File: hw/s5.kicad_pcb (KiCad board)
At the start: 4 copper layers, 130 x 80 mm, 218 parts, among them J1 Conn_01x03, J12 USB_C_Receptacle, J2 LPJG0926HENL, J3 LPJG0926HENL, J4 LPJG0926HENL, J5 LPJG0926HENL, J6 LPJG0926HENL, J7 Conn_01x03, J8 microSD, Q1 NMOS, Q2 NMOS, Q3 NMOS, Q4 NMOS, Q5 NMOS, SW2 SW_Push, U1 KSZ9477S, U10 TPS3823, U11 TLV62569, U12 AP2112K-1.8, U13 TPS23861, U14 LM5122, U2 AMS1117-3.3, U3 AP2112K-2.5, U4 AP2112K-1.2, U6 TPS54560, U7 T113-S3, U8 W25N02JWZEIF, U9 TPS23861, Y1 25MHz, Y2 24MHz, Y3 32.768kHz

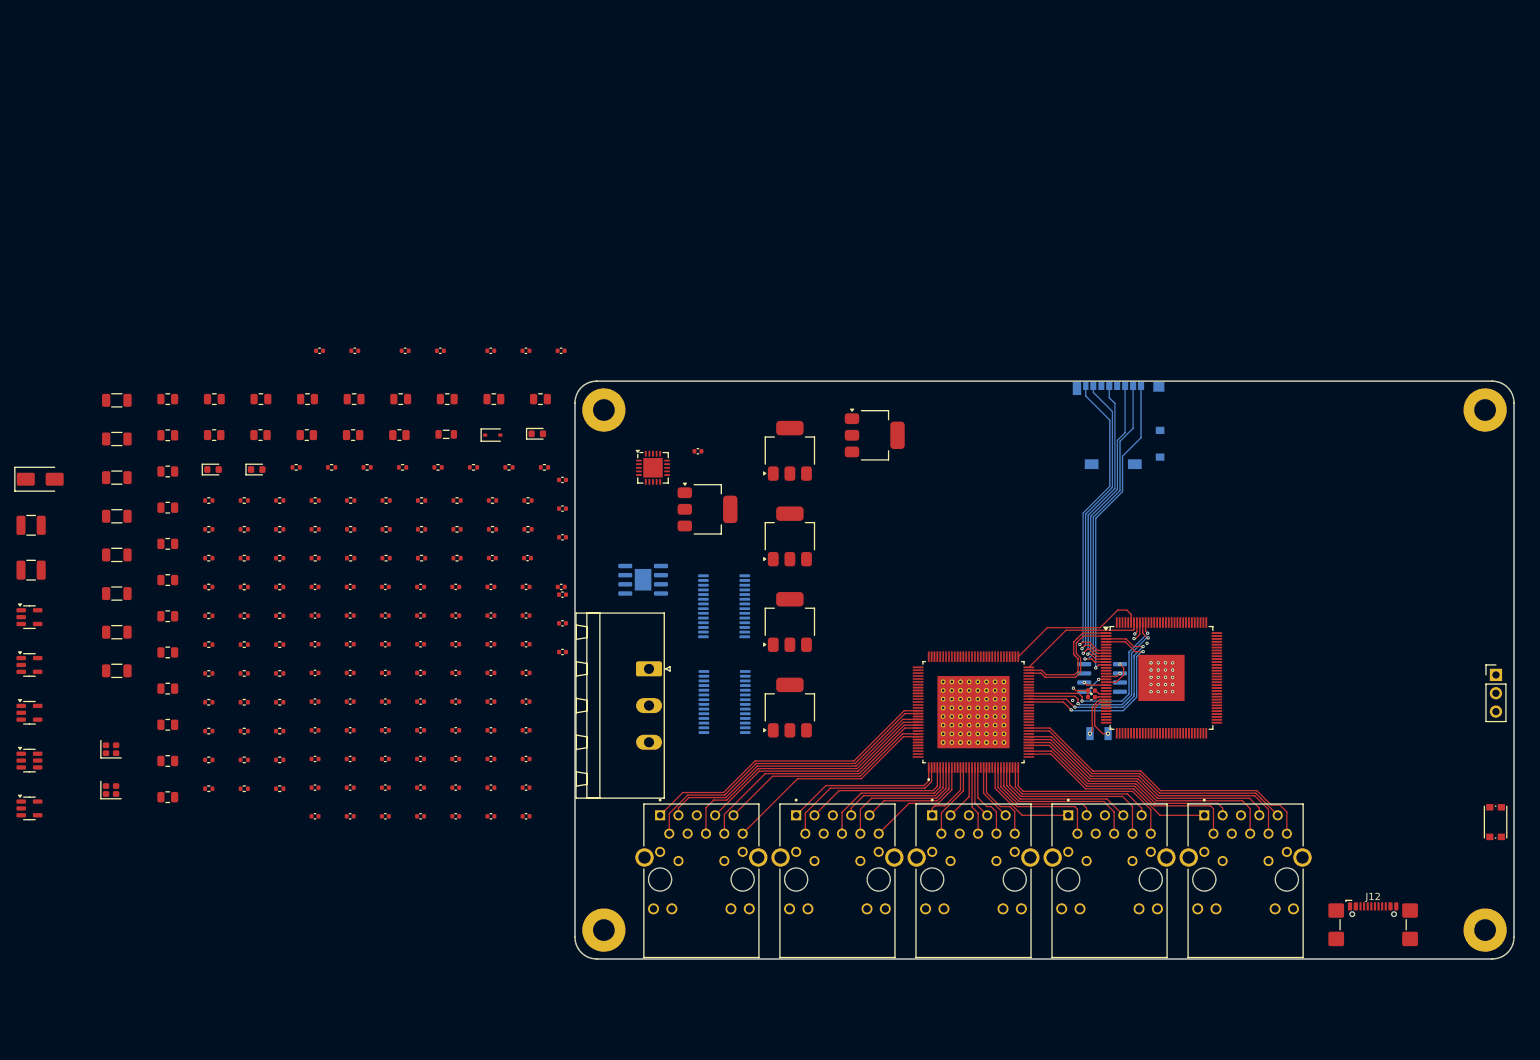
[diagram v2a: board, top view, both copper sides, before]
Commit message: hw: normalize vendor 3D models, self-contained vendor-3d/, KiCad 10 migration
- All connector/chip STEP models rotated upright and origin-corrected
- Custom models moved to vendor-3d/ with ${KIPRJMOD} paths (portable)
- Board opened/saved in KiCad 10; pre-10 backup kept as s5.kicad_pcb.bak-pre-k10
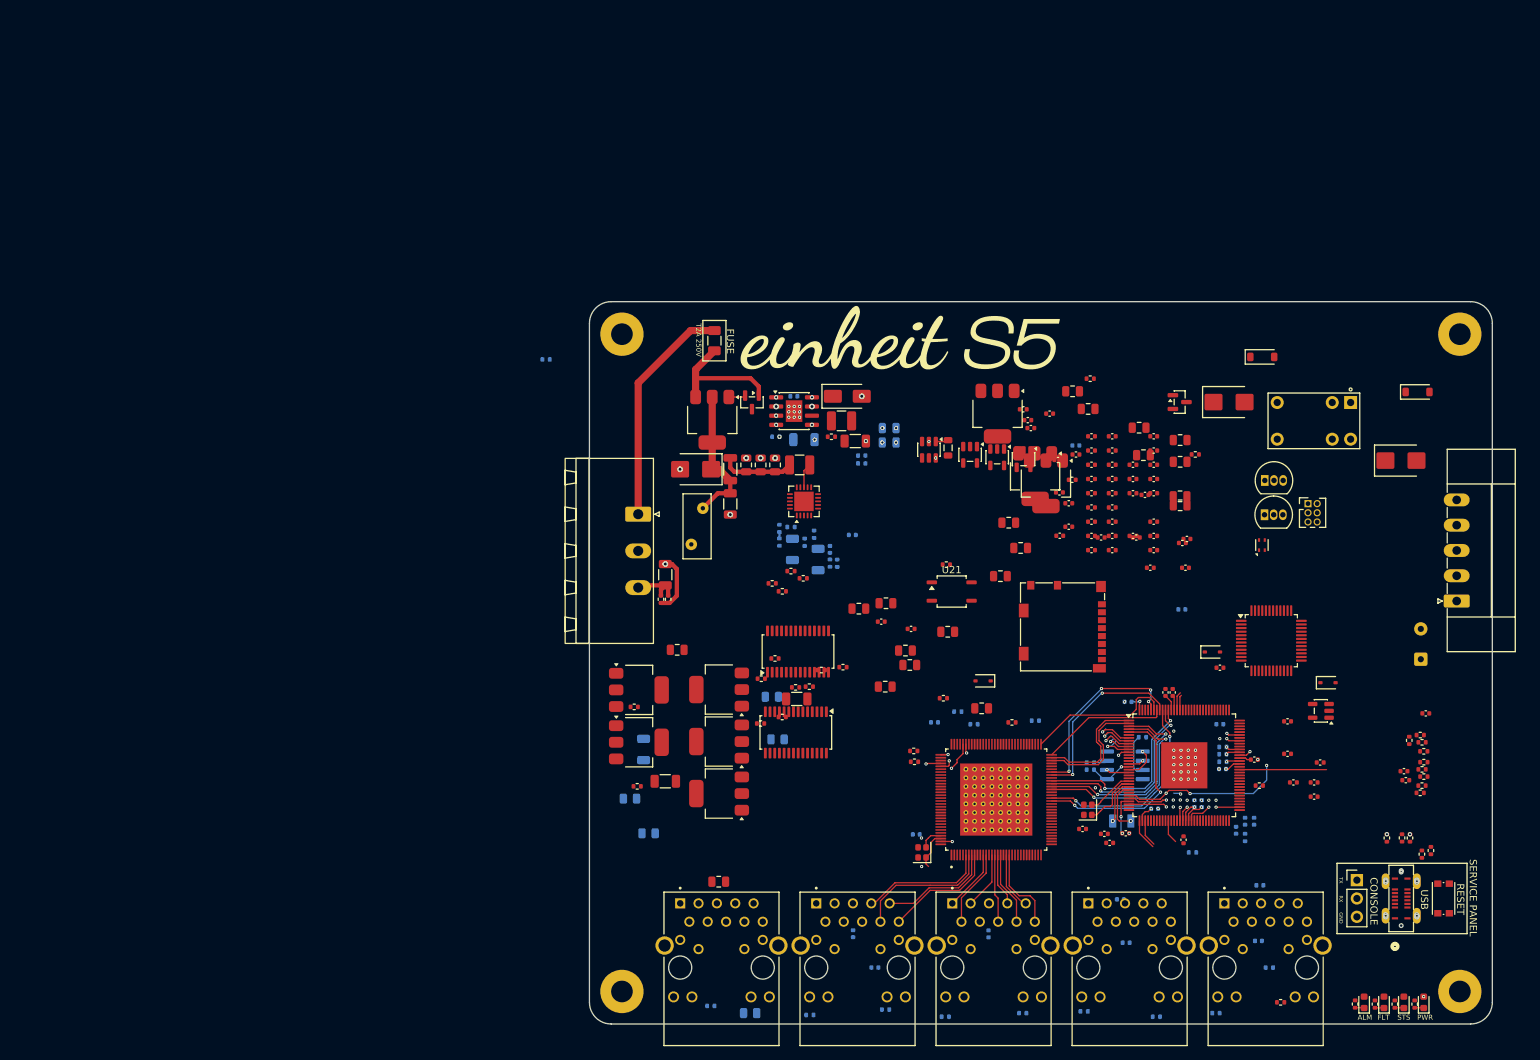
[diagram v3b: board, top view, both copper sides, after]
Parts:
- removed REF** (x4): MountingHole_3mm_Pad, MountingHole:MountingHole_3mm_Pad
- added C111: 100nF, Capacitor_SMD:C_0402_1005Metric, F.Cu at (160.8, 86.4)
- added C112: 100nF, Capacitor_SMD:C_0402_1005Metric, F.Cu at (167.6, 87.4)
- added C113: 10uF, Capacitor_SMD:C_0805_2012Metric, F.Cu at (167.3, 76.2)
- added C114: 100nF, Capacitor_SMD:C_0402_1005Metric, F.Cu at (163.6, 72.6)
- added C115: 10uF, Capacitor_SMD:C_0805_2012Metric, F.Cu at (152.4, 66.4)
- added C116: 100nF, Capacitor_SMD:C_0402_1005Metric, F.Cu at (163.6, 74.6)
- added C117: 100nF, Capacitor_SMD:C_0402_1005Metric, F.Cu at (163.6, 76.6)
- added C118: 100nF, Capacitor_SMD:C_0402_1005Metric, F.Cu at (163.6, 78.5)
- added C119: 100nF, Capacitor_SMD:C_0402_1005Metric, F.Cu at (163.6, 80.5)
- added C120: 4.7uF, Capacitor_SMD:C_0805_2012Metric, F.Cu at (167.3, 82.2)
- added C121: 100nF, Capacitor_SMD:C_0402_1005Metric, F.Cu at (198.5, 120.2)
- added C122: 100nF, Capacitor_SMD:C_0402_1005Metric, F.Cu at (163.6, 84.5)
- added C123: 100nF, Capacitor_SMD:C_0402_1005Metric, F.Cu at (163.6, 86.4)
- added C124: 100nF, Capacitor_SMD:C_0402_1005Metric, F.Cu at (163.6, 88.4)
- added C125: 4.7nF, Capacitor_SMD:C_1206_3216Metric, F.Cu at (96.0, 91.8)
- added D50: SMBJ30A, Diode_SMD:D_SMB, F.Cu at (100.2, 77.2)
- added D51: BZX84C12, Package_TO_SOT_SMD:SOT-23, F.Cu at (108.0, 67.9)
- added D52: BAT54, Diode_SMD:D_SOD-323, F.Cu at (171.8, 102.5)
- added D53: BAT54, Diode_SMD:D_SOD-323, F.Cu at (187.8, 106.8)
- added D54: 1N4148W, Diode_SMD:D_SOD-123, F.Cu at (200.2, 66.5)
- added D55: SMBJ33CA, Diode_SMD:D_SMB, F.Cu at (174.1, 67.9)
- added D56: 1N4148W, Diode_SMD:D_SOD-123, F.Cu at (178.7, 61.6)
- added D57: SMBJ33CA, Diode_SMD:D_SMB, F.Cu at (197.8, 76.0)
- added D6: LED, LED_SMD:LED_0603_1608Metric, F.Cu at (192.8, 151.0)
- added F1: Fuse_2A_TL, Fuse:Fuse_1206_3216Metric, F.Cu at (102.8, 59.4)
- added FB1: BLM31PG601SN1, Inductor_SMD:L_1206_3216Metric, F.Cu at (105.0, 77.2)
- added J10: SWD_2x3, Connector_PinHeader_1.27mm:PinHeader_2x03_P1.27mm_Vertical, F.Cu at (185.0, 82.0)
- added J11: MC1,5/5-GF-3,5_1843826, Connector_Phoenix_MC:PhoenixContact_MC_1,5_5-GF-3.5_1x05_P3.50mm_Horizontal_ThreadedFlange, F.Cu at (205.6, 95.4)
- added K1: HFD23-024-1ZS, connectors:Relay_HFD23_1C_THT, F.Cu at (185.8, 70.5)
- added MH1: MountingHole_M3_PE, MountingHole:MountingHole_3mm_Pad, F.Cu at (90.0, 149.5)
- added MH2: MountingHole_M3_PE, MountingHole:MountingHole_3mm_Pad, F.Cu at (90.0, 58.5)
- added MH3: MountingHole_M3_PE, MountingHole:MountingHole_3mm_Pad, F.Cu at (206.0, 58.5)
- added MH4: MountingHole_M3_PE, MountingHole:MountingHole_3mm_Pad, F.Cu at (206.0, 149.5)
- added Q50: BSP315P, Package_TO_SOT_SMD:SOT-223-3_TabPin2, F.Cu at (102.5, 70.3)
- added Q60: 2N7002, Package_TO_SOT_SMD:SOT-23, F.Cu at (167.2, 67.9)
- added R66: 270, Resistor_SMD:R_0402_1005Metric, F.Cu at (197.0, 151.2)
- added R67: 270, Resistor_SMD:R_0402_1005Metric, F.Cu at (194.2, 151.2)
- added R68: 10k, Resistor_SMD:R_0402_1005Metric, F.Cu at (200.8, 121.0)
- added R69: 10k, Resistor_SMD:R_0402_1005Metric, F.Cu at (200.5, 122.0)
- added R70: 10k, Resistor_SMD:R_0402_1005Metric, F.Cu at (154.8, 64.7)
- added R71: 1k, Resistor_SMD:R_0402_1005Metric, F.Cu at (178.2, 121.0)
- added R72: 4.7k, Resistor_SMD:R_0402_1005Metric, F.Cu at (201.0, 117.8)
- added R73: 4.7k, Resistor_SMD:R_0402_1005Metric, F.Cu at (201.0, 119.8)
- added R74: 4.7k, Resistor_SMD:R_0402_1005Metric, F.Cu at (200.8, 118.8)
- added R75: 270, Resistor_SMD:R_0402_1005Metric, F.Cu at (191.5, 151.2)
- added R76: 100k, Resistor_SMD:R_0402_1005Metric, F.Cu at (200.8, 115.0)
- added R77: 4.7k, Resistor_SMD:R_0402_1005Metric, F.Cu at (201.0, 116.2)
- added R78: 10k, Resistor_SMD:R_0402_1005Metric, F.Cu at (200.5, 114.0)
- added R79: 1M, Resistor_SMD:R_0402_1005Metric, F.Cu at (96.4, 95.2)
- added R80: 0R, Resistor_SMD:R_0402_1005Metric, F.Cu at (95.4, 95.2)
- added RV1: MOV_S14K30_DNP, Varistor:RV_Disc_D9mm_W3.9mm_P5mm, F.Cu at (101.2, 82.6)
- added TS1: Thermostat_NO_95C, Connector_Wire:SolderWire-0.25sqmm_1x02_P4.2mm_D0.65mm_OD1.7mm, F.Cu at (200.6, 103.5)
- added U15: DS18B20, Package_TO_SOT_THT:TO-92_Inline, F.Cu at (179.0, 83.5)
- added U16: DS18B20, Package_TO_SOT_THT:TO-92_Inline, F.Cu at (179.0, 78.8)
- added U17: SHT40-AD1B, Sensor_Humidity:Sensirion_DFN-4_1.5x1.5mm_P0.8mm_SHT4x_NoCentralPad, F.Cu at (178.6, 87.7)
- added U18: TPS7B6933QDCYRQ1, Package_TO_SOT_SMD:SOT-223-3_TabPin2, F.Cu at (148.7, 79.2)
- added U19: STM32G071CBTx, Package_QFP:LQFP-48_7x7mm_P0.5mm, F.Cu at (179.9, 100.9)
- added U20: TPS7B6933QDCYRQ1, Package_TO_SOT_SMD:SOT-223-3_TabPin2, F.Cu at (147.2, 78.2)
- added U21: EL357N, Package_SO:SOP-4_3.8x4.1mm_P2.54mm, F.Cu at (135.7, 94.1)
- C1: value 100uF -> 10uF
- C10, C9: value 22uF -> 10uF
- C100, C101, C19, C60, C67, C68, C69, C70, C71, C73, C74, C75, C77, C8, C88, C92, C99, R19, R26, R27, R28, R29, R30, R31, R32, R54, R57, R58, R7: moved to B.Cu
- C103, C104: value 10uF -> 100nF
- C105, C106: value 18pF -> 10uF
- C107, C108: value 100nF -> 18pF
- C11, C12: value 100nF -> 22uF
- C13: value 15nF -> 100nF; moved to B.Cu
- C14: value 2.2uF -> 100nF; moved to B.Cu
- C15: value 2.2uF -> 15nF
- C16, C17: value 22uF -> 2.2uF
- C18, C21, C22: value 10uF -> 22uF
- C2: value 4.7uF -> 10uF
- C20: value 22uF -> 10uF; moved to B.Cu
- C3: value 100nF -> 100uF
- C30, C31: value 100nF -> 10uF; footprint Capacitor_SMD:C_0402_1005Metric -> Capacitor_SMD:C_0805_2012Metric
- C4: value 100nF -> 4.7uF; moved to B.Cu
- C5: value 10nF -> 100nF; moved to B.Cu
- C6: value 10uF -> 100nF; moved to B.Cu
- C62, C63: value 15pF -> 100nF
- C64: value 10uF -> 15pF
- C65: value 100nF -> 15pF; moved to B.Cu
- C66: value 100nF -> 10uF; moved to B.Cu
- C7: value 10uF -> 10nF; moved to B.Cu
- C79, C80: value 1uF -> 100nF; moved to B.Cu
- C81: value 100nF -> 1uF
- C82: value 100nF -> 1uF; moved to B.Cu
- J1: value Conn_01x03 -> MSTB2,5/3-GF-5,08_1776511
- J12: value USB_C_Receptacle -> USB-C_2171820001; footprint connectors:USB_C_GCT_USB4110 -> connectors:CONN_2171820001_MOL
- J2, J3, J4, J5, J6: value LPJG0926HENL -> LINK-PP_LPJG0926HENL
- J8, U13, U6, U9: moved to F.Cu
- R1: value 150k -> 100k; moved to B.Cu
- R10: value 52.3k -> 100k; moved to B.Cu
- R11: value 10k -> 13k; moved to B.Cu
- R12: value 50k -> 24.9k
- R13: value 100k -> 52.3k; moved to B.Cu
- R14: value 6.04k -> 10k; moved to B.Cu
- R15: value 191 -> 50k
- R16: value 10k -> 100k
- R17: value 4.7k -> 6.04k; moved to B.Cu
- R18: value 4.7k -> 191
- R2: value 100k -> 150k
- R20, R21: value 10k -> 4.7k
- R22: value 1k -> 10k
- R23, R24: value 150 -> 10k; moved to B.Cu
- R25: value 150 -> 1k; moved to B.Cu
- R3: value 6.8k -> 100k; moved to B.Cu
- R33: value 10k -> 150
- R34: value 47 -> 150; moved to B.Cu
- R35: value 0.25 -> 150; moved to B.Cu
- R36, R39, R42, R45: value 22 -> 47
- R37, R40, R43: value 47 -> 0.25
- R38, R41, R44: value 0.25 -> 22; moved to B.Cu
- R4: value 33k -> 6.8k; moved to B.Cu
- R46: value 22 -> 0.25; moved to B.Cu
- R48: value 10k -> 22
- R49: value 47 -> 22
- R5: value 383k -> 33k; moved to B.Cu
- R50: value 0.25 -> 47; moved to B.Cu
- R51: value 22 -> 0.25
- R53: value 4.7k -> 22; moved to B.Cu
- R55: value 240 -> 4.7k; moved to B.Cu
- R56: value 10k -> 240; moved to B.Cu
- R59, R60: value 27 -> 10k
- R6: value 10k -> 383k
- R61, R62: value 5.1k -> 27
- R63, R64: value 270 -> 5.1k
- R8: value 100k -> 10k; moved to B.Cu
- R9: value 24.9k -> 100k; moved to B.Cu
- moved D4 180.6 mm to (198.2, 151.0), turned to 90 degrees
- moved U10 178.8 mm to (186.8, 110.7), turned to 180 degrees
- moved D3 177.6 mm to (201.0, 151.0), turned to 90 degrees
- moved R63 168.8 mm to (200.8, 130.5), turned to -90 degrees
- moved R61 165.3 mm to (195.9, 128.2), turned to 90 degrees
- moved R64 164.4 mm to (202.0, 130.0), turned to -90 degrees
- moved R46 158.9 mm to (179.6, 146.2), turned to 180 degrees
- moved R59 158.4 mm to (198.0, 128.2), turned to -90 degrees
- moved R33 156.1 mm to (181.2, 151.0)
- moved R32 151.4 mm to (172.2, 152.5), turned to 180 degrees
- moved R31 149.4 mm to (164.0, 153.0), turned to 180 degrees
- moved R65 145.8 mm to (199.8, 151.2), turned to -90 degrees
- moved C72 144.7 mm to (201.3, 111.0)
- moved C21 143.9 mm to (161.6, 71.5)
- moved C26 141.6 mm to (162.2, 75.2)
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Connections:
- C1 pad 1: VIN_24V -> VIN_PROT
- C10 pad 1: VIN_24V -> VBUS_48V
- C100 pad 1: VDD_1V8 -> VDD_CORE
- C103 pad 1: VDD_CORE -> VDD_1V8
- C104 pad 1: VDD_3V3 -> VDD_1V8
- C105 pad 1: T113_DXIN -> VDD_CORE
- C106 pad 1: T113_DXOUT -> VDD_3V3
- C107 pad 1: SOC_RESET_N -> T113_DXIN
- C108 pad 1: VDD_3V3 -> T113_DXOUT
- C109 pad 1: VDD_3V3 -> SOC_RESET_N
- C11 pad 1: BOOT -> VIN_24V
- C11 pad 2: SW_NODE -> GND
- C12 pad 1: SS_TR -> VIN_24V
- C13 pad 1: COMP_MID -> BOOT
- C13 pad 2: GND -> SW_NODE
- C14 pad 1: VIN_24V -> SS_TR
- C15 pad 1: VIN_24V -> COMP_MID
- C16 pad 1: VDD_5V -> VIN_24V
- C17 pad 1: VDD_5V -> VIN_24V
- C19 pad 1: VDD_CORE -> VDD_5V
- C2 pad 1: BOOST_VCC -> VIN_24V
- C20 pad 1: VDD_CORE -> VDD_5V
- C21 pad 1: VDD_1V8 -> VDD_CORE
- C22 pad 1: VDD_1V8 -> VDD_CORE
- C23 pad 1: VIN_24V -> VDD_1V8
- C24 pad 1: VDD_5V -> VDD_1V8
- C25 pad 1: VDD_3V3 -> VIN_24V
- C26 pad 1: VDD_2V5 -> VDD_5V
- C27 pad 1: VDD_1V2 -> VDD_3V3
- C28 pad 1: VDD_CORE -> VDD_2V5
- C29 pad 1: VDD_1V8 -> VDD_1V2
- C3 pad 1: BST_BOOST -> VIN_24V
- C3 pad 2: BOOST_SW -> GND
- C30 pad 1: VDD_2V5 -> VDD_CORE
- C31 pad 1: VDD_2V5 -> VDD_1V8
- C39 pad 1: VDD_1V2 -> VDD_2V5
- C4 pad 1: BOOST_SS -> BOOST_VCC
- C40 pad 1: VDD_1V2 -> VDD_2V5
- C5 pad 1: BOOST_COMP_MID -> BST_BOOST
- C5 pad 2: GND -> BOOST_SW
- C59 pad 1: VDD_3V3 -> VDD_1V2
- C6 pad 1: VBUS_48V -> BOOST_SS
- C60 pad 1: VDD_3V3 -> VDD_1V2
- C62 pad 1: KSZ_XI -> VDD_3V3
- C63 pad 1: KSZ_XO -> VDD_3V3
- C64 pad 1: KSZ_RESET_N -> KSZ_XI
- C65 pad 1: P1_CT1 -> KSZ_XO
- C66 pad 1: P1_CT2 -> KSZ_RESET_N
- C67 pad 1: P2_CT1 -> P1_CT1
- C68 pad 1: P2_CT2 -> P1_CT2
- C69 pad 1: P3_CT1 -> P2_CT1
- C7 pad 1: VBUS_48V -> BOOST_COMP_MID
- C70 pad 1: P3_CT2 -> P2_CT2
- C71 pad 1: P4_CT1 -> P3_CT1
- C72 pad 1: P4_CT2 -> P3_CT2
- C73 pad 1: P5_CT1 -> P4_CT1
- C74 pad 1: P5_CT2 -> P4_CT2
- C75 pad 1: VDD_3V3 -> P5_CT1
- C76 pad 1: VBUS_48V -> P5_CT2
- C77 pad 1: VDD_3V3 -> VDD_3V3_PSE
- C79 pad 1: N$12 -> VDD_3V3_PSE
- C80 pad 1: N$13 -> VBUS_48V
- C81 pad 1: VDD_3V3 -> T113_LDOA_OUT
- C82 pad 1: VDD_3V3 -> T113_LDOB_OUT
- C9 pad 1: VIN_24V -> VBUS_48V
- C93 pad 1: VDD_CORE -> VDD_3V3
- C94 pad 1: VDD_CORE -> VDD_3V3
- C99 pad 1: VDD_1V8 -> VDD_CORE
- J1 pad 1: VIN_24V -> VIN_RAW
- J2 pad 15: N$2 -> P1_GRN_A
- J2 pad 17: N$3 -> P1_YEL_A
- J3 pad 15: N$4 -> P2_GRN_A
- J3 pad 17: N$5 -> P2_YEL_A
- J4 pad 15: N$6 -> P3_GRN_A
- J4 pad 17: N$7 -> P3_YEL_A
- J5 pad 15: N$8 -> P4_GRN_A
- J5 pad 17: N$9 -> P4_YEL_A
- J6 pad 15: N$10 -> P5_GRN_A
- J6 pad 17: N$11 -> P5_YEL_A
- R1 pad 1: BOOST_RT -> RP_GATE
- R10 pad 1: VDD_5V -> VIN_24V
- R10 pad 2: FB_5V -> MAIN_EN
- R11 pad 1: FB_5V -> MAIN_EN
- R12 pad 1: VDD_CORE -> COMP
- R12 pad 2: FB_0V9 -> COMP_MID
- R13 pad 1: FB_0V9 -> VDD_5V
- R13 pad 2: GND -> FB_5V
- R14 pad 1: KSZ_ISET -> FB_5V
- R15 pad 1: KSZ_S_REXT -> VDD_CORE
- R15 pad 2: GND -> FB_0V9
- R16 pad 1: VDD_3V3 -> FB_0V9
- R16 pad 2: KSZ_RESET_N -> GND
- R17 pad 1: VDD_3V3 -> KSZ_ISET
- R17 pad 2: SPI_MOSI -> GND
- R18 pad 1: VDD_3V3 -> KSZ_S_REXT
- R18 pad 2: SPI_CS_N -> GND
- R19 pad 2: INTRP_N -> KSZ_RESET_N
- R2 pad 1: VIN_24V -> BOOST_RT
- R2 pad 2: BOOST_UVLO -> GND
- R20 pad 2: PME_N -> SPI_MOSI
- R21 pad 2: SYNCLKO -> SPI_CS_N
- R22 pad 1: IBA -> VDD_3V3
- R22 pad 2: GND -> INTRP_N
- R23 pad 2: N$2 -> PME_N
- R24 pad 2: N$3 -> SYNCLKO
- R25 pad 1: VDD_3V3 -> IBA
- R25 pad 2: N$4 -> GND
- R26 pad 2: N$5 -> P1_GRN_A
- R27 pad 2: N$6 -> P1_YEL_A
- R28 pad 2: N$7 -> P2_GRN_A
- R29 pad 2: N$8 -> P2_YEL_A
- R3 pad 1: BOOST_UVLO -> VIN_24V
- R3 pad 2: GND -> BOOST_UVLO
- R30 pad 2: N$9 -> P3_GRN_A
- R31 pad 2: N$10 -> P3_YEL_A
- R32 pad 2: N$11 -> P4_GRN_A
- R33 pad 2: U9_RESET -> P4_YEL_A
- R34 pad 1: VBUS_48V -> VDD_3V3
- R34 pad 2: U9_DRAIN16 -> P5_GRN_A
- R35 pad 1: U9_SRC15 -> VDD_3V3
- R35 pad 2: POE_VP_1 -> P5_YEL_A
- R36 pad 1: U9_SRC15 -> VBUS_48V
- R36 pad 2: U9_SEN15 -> U9_DRAIN16
- R37 pad 1: VBUS_48V -> U9_SRC15
- R37 pad 2: U9_DRAIN20 -> POE_VP_1
- R38 pad 1: U9_SRC19 -> U9_SRC15
- R38 pad 2: POE_VP_2 -> U9_SEN15
- R39 pad 1: U9_SRC19 -> VBUS_48V
- R39 pad 2: U9_SEN19 -> U9_DRAIN20
- R4 pad 1: BOOST_ILIM -> BOOST_UVLO
- R40 pad 1: VBUS_48V -> U9_SRC19
- R40 pad 2: U9_DRAIN9 -> POE_VP_2
- R41 pad 1: U9_SRC8 -> U9_SRC19
- R41 pad 2: POE_VP_3 -> U9_SEN19
- R42 pad 1: U9_SRC8 -> VBUS_48V
- R42 pad 2: U9_SEN8 -> U9_DRAIN9
- R43 pad 1: VBUS_48V -> U9_SRC8
- R43 pad 2: U9_DRAIN13 -> POE_VP_3
- R44 pad 1: U9_SRC12 -> U9_SRC8
- R44 pad 2: POE_VP_4 -> U9_SEN8
- R45 pad 1: U9_SRC12 -> VBUS_48V
- R45 pad 2: U9_SEN12 -> U9_DRAIN13
- R46 pad 1: U9_KSENSA -> U9_SRC12
- R46 pad 2: GND -> POE_VP_4
- R47 pad 1: U9_KSENSB -> U9_SRC12
- R47 pad 2: GND -> U9_SEN12
- R48 pad 1: VDD_3V3 -> U9_KSENSA
- R48 pad 2: U13_RESET -> GND
- R49 pad 1: VBUS_48V -> U9_KSENSB
- R49 pad 2: U13_DRAIN16 -> GND
- R5 pad 1: VBUS_48V -> BOOST_ILIM
- R5 pad 2: BOOST_FB -> GND
- R50 pad 1: U13_SRC15 -> VBUS_48V
- R50 pad 2: POE_VP_5 -> U13_DRAIN16
- R51 pad 2: U13_SEN15 -> POE_VP_5
- R52 pad 1: U13_KSENSA -> U13_SRC15
- R52 pad 2: GND -> U13_SEN15
- R53 pad 1: VDD_3V3 -> U13_KSENSA
- R53 pad 2: PSE_I2C_SDA -> GND
- R54 pad 2: PSE_I2C_SCL -> PSE_I2C_SDA
- R55 pad 1: T113_DZQ -> VDD_3V3
- R55 pad 2: GND -> PSE_I2C_SCL
- R56 pad 1: VDD_3V3 -> T113_DZQ
- R56 pad 2: SOC_RESET_N -> GND
- R57 pad 2: FLASH_WP -> SOC_RESET_N
- R58 pad 2: FLASH_HOLD -> FLASH_WP
- R59 pad 1: USB_DP -> VDD_3V3
- R59 pad 2: USB_CONN_DP -> FLASH_HOLD
- R6 pad 1: BOOST_FB -> VBUS_48V
- R6 pad 2: GND -> BOOST_FB
- R60 pad 1: USB_DM -> VDD_3V3_SB
- R60 pad 2: USB_CONN_DM -> STM_WD_RST
- R61 pad 1: USB_CC1 -> USB_DP
- R61 pad 2: GND -> USB_CONN_DP
- R62 pad 1: USB_CC2 -> USB_DM
- R62 pad 2: GND -> USB_CONN_DM
- R63 pad 1: VDD_3V3 -> USB_CC1
- R63 pad 2: LED_PWR_A -> GND
- R64 pad 1: VDD_3V3 -> USB_CC2
- R64 pad 2: LED_STA_A -> GND
- R65 pad 2: LED_FAULT_A -> LED_PWR_A
- R7 pad 1: BOOST_COMP -> BOOST_FB
- R7 pad 2: BOOST_COMP_MID -> GND
- R8 pad 1: VIN_24V -> BOOST_COMP
- R8 pad 2: BOOST_PG -> BOOST_COMP_MID
- R9 pad 1: COMP -> VIN_24V
- R9 pad 2: COMP_MID -> BOOST_PG
- U10 pad 1: SOC_RESET_N -> STM_WD_RST
- U10 pad 3: VDD_3V3 -> VDD_3V3_SB
- U10 pad 4: VDD_3V3 -> VDD_3V3_SB
- U10 pad 5: WDI -> STM_WDI
- U13 pad 1: VDD_3V3 -> VDD_3V3_PSE
- U13 pad 2: U13_RESET -> PSE_RESET_N
- U13 pad 23: VDD_3V3 -> VDD_3V3_PSE
- U13 pad 24: VDD_3V3 -> VDD_3V3_PSE
- U14 pad 10: BOOST_VCC1 -> BOOST_VCC
- U14 pad 19: BOOST_PG1 -> BOOST_PG
- U14 pad 2: BOOST_ILIM1 -> BOOST_ILIM
- U14 pad 6: BOOST_RT1 -> BOOST_RT
- U14 pad 7: BOOST_SS1 -> BOOST_SS
- U6 pad 3: VIN_24V -> MAIN_EN
- U7 pad 28: N$12 -> T113_LDOA_OUT
- U7 pad 30: N$13 -> T113_LDOB_OUT
- U7 pad 72: (no net) -> MCU_BOOT0_CTL
- U7 pad 73: (no net) -> MCU_NRST
- U7 pad 74: (no net) -> SUP_HEARTBEAT
- U7 pad 75: (no net) -> SUP_T113_TO_MCU
- U7 pad 76: (no net) -> SUP_MCU_TO_T113
- U7 pad 80: WDI -> (no net)
- U9 pad 1: VDD_3V3 -> VDD_3V3_PSE
- U9 pad 2: U9_RESET -> PSE_RESET_N
- U9 pad 24: VDD_3V3 -> VDD_3V3_PSE
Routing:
- net PE: track 0.00 -> 435.0 mm
- net SPI_CS_N: track 0.00 -> 52.6 mm, vias 0 -> 2
- net P4_DN: track 43.5 -> 0.00 mm
- net P5_AN: track 43.0 -> 0.00 mm
- net P5_AP: track 41.7 -> 0.00 mm
- net SD_D2: track 43.2 -> 1.61 mm
- net P4_CN: track 40.7 -> 0.00 mm
- net SD_D3: track 43.9 -> 4.55 mm
- net P4_DP: track 39.3 -> 0.00 mm
- net P5_BP: track 39.3 -> 0.00 mm
- net SD_CMD: track 42.1 -> 3.39 mm
- net SD_D0: track 43.3 -> 4.77 mm
- net SD_D1: track 43.1 -> 4.85 mm
- net SD_CLK: track 43.0 -> 4.79 mm
- net P4_BN: track 37.9 -> 0.00 mm
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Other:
- board size 130 x 80 mm -> 125 x 100 mm
- board text added: "ALM"
- board text added: "CONSOLE"
- board text added: "FLT"
- board text added: "FUSE"
- board text added: "GND"
- board text added: "PWR"
- board text added: "RESET"
- board text added: "RX"
- board text added: "SERVICE PANEL"
- board text added: "STS"
- board text added: "T2A 250V"
- board text added: "TX"
- board text added: "USB"
